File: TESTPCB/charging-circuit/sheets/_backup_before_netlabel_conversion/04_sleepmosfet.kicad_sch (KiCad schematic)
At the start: 8 parts, among them P3 1.27mm/1*3p, Q8 CJQ4435, U4 TPL5110DDCT

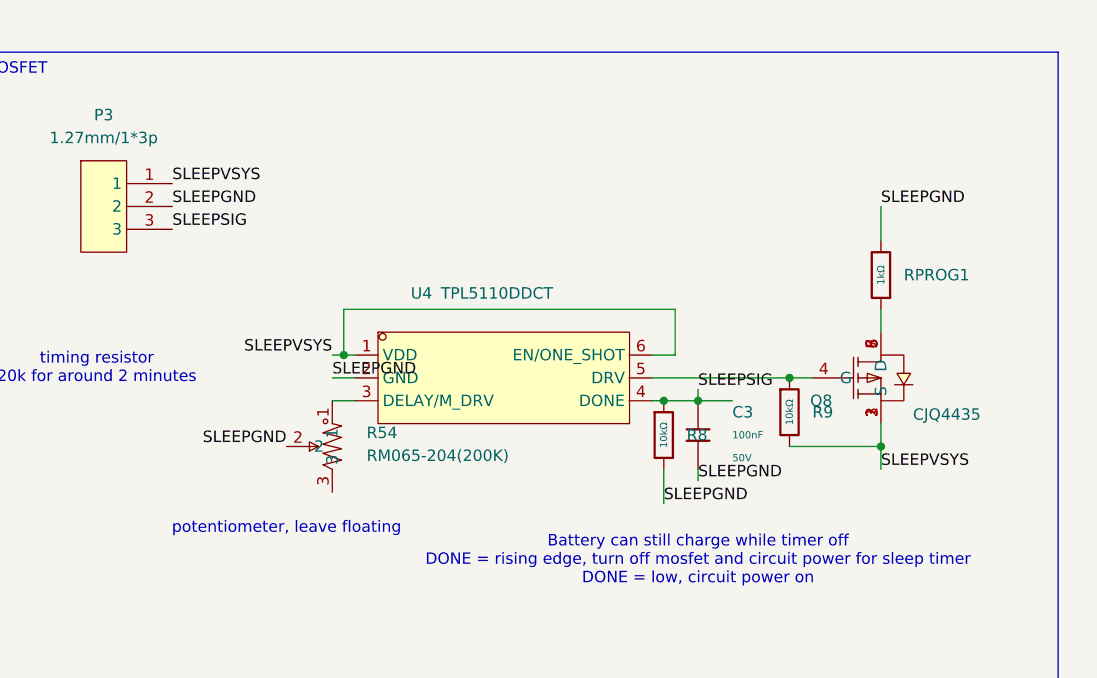
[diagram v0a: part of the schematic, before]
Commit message: Fixed formatting issues, now the hierachal sheets are all labeled as net labels and when we want to expose their pins we will make them into hierchal or global pins
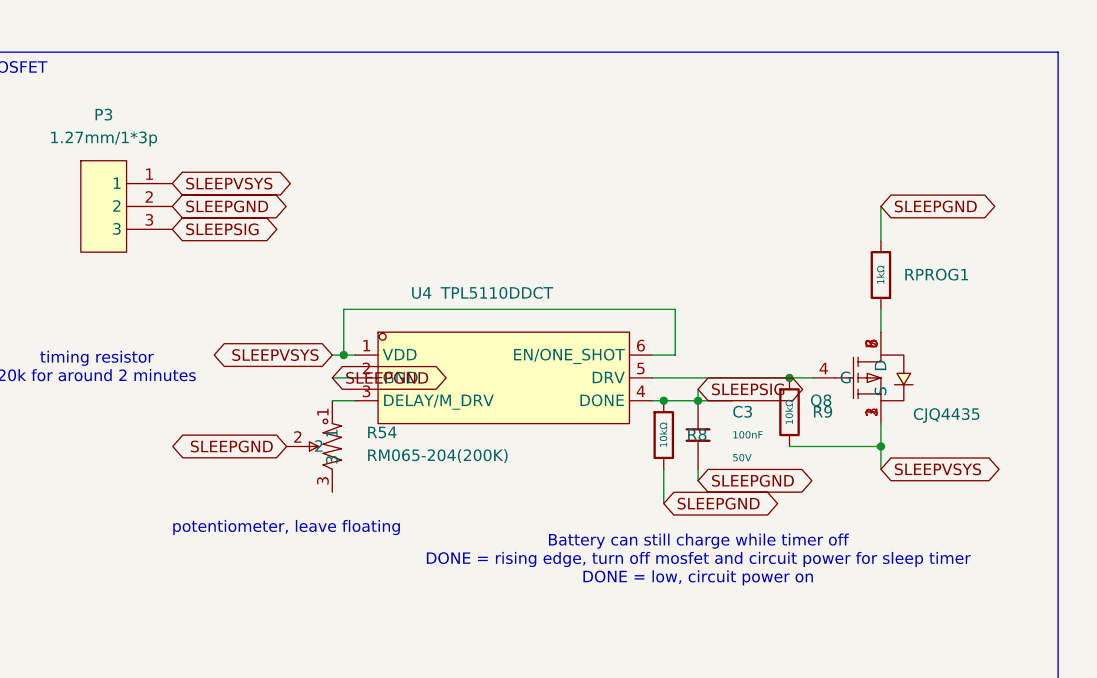
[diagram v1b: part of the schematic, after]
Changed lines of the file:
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@@
 		)
 	)
-	(label "SLEEPGND"
+	(global_label "SLEEPGND"
+		(shape bidirectional)
 		(at 186.69 90.17 0)
 		(effects
@@
 			(justify left bottom)
 		)
-	)
-	(label "SLEEPSIG"
+		(property "Intersheetrefs" "${INTERSHEET_REFS}"
+			(at 186.69 90.17 0)
+			(effects
+				(font
+					(size 1.27 1.27)
+				)
+				(hide yes)
+			)
+		)
+	)
+	(global_label "SLEEPSIG"
+		(shape bidirectional)
 		(at 166.37 110.49 0)
 		(effects
@@
 			(justify left bottom)
 		)
-	)
-	(label "SLEEPVSYS"
+		(property "Intersheetrefs" "${INTERSHEET_REFS}"
+			(at 166.37 110.49 0)
+			(effects
+				(font
+					(size 1.27 1.27)
+				)
+				(hide yes)
+			)
+		)
+	)
+	(global_label "SLEEPVSYS"
+		(shape bidirectional)
 		(at 107.95 87.63 0)
 		(effects
@@
 			(justify left bottom)
 		)
-	)
-	(label "SLEEPGND"
+		(property "Intersheetrefs" "${INTERSHEET_REFS}"
+			(at 107.95 87.63 0)
+			(effects
+				(font
+					(size 1.27 1.27)
+				)
+				(hide yes)
+			)
+		)
+	)
+	(global_label "SLEEPGND"
+		(shape bidirectional)
 		(at 107.95 90.17 0)
 		(effects
@@
 			(justify left bottom)
 		)
-	)
-	(label "SLEEPGND"
+		(property "Intersheetrefs" "${INTERSHEET_REFS}"
+			(at 107.95 90.17 0)
+			(effects
+				(font
+					(size 1.27 1.27)
+				)
+				(hide yes)
+			)
+		)
+	)
+	(global_label "SLEEPGND"
+		(shape bidirectional)
 		(at 120.65 116.84 180)
 		(effects
@@
 			(justify right bottom)
 		)
-	)
-	(label "SLEEPSIG"
+		(property "Intersheetrefs" "${INTERSHEET_REFS}"
+			(at 120.65 116.84 0)
+			(effects
+				(font
+					(size 1.27 1.27)
+				)
+				(hide yes)
+			)
+		)
+	)
+	(global_label "SLEEPSIG"
+		(shape bidirectional)
 		(at 107.95 92.71 0)
 		(effects
@@
 			(justify left bottom)
 		)
-	)
-	(label "SLEEPGND"
+		(property "Intersheetrefs" "${INTERSHEET_REFS}"
+			(at 107.95 92.71 0)
+			(effects
+				(font
+					(size 1.27 1.27)
+				)
+				(hide yes)
+			)
+		)
+	)
+	(global_label "SLEEPGND"
+		(shape bidirectional)
 		(at 125.73 109.22 0)
 		(effects
@@
 			(justify left bottom)
 		)
-	)
-	(label "SLEEPVSYS"
+		(property "Intersheetrefs" "${INTERSHEET_REFS}"
+			(at 125.73 109.22 0)
+			(effects
+				(font
+					(size 1.27 1.27)
+				)
+				(hide yes)
+			)
+		)
+	)
+	(global_label "SLEEPVSYS"
+		(shape bidirectional)
 		(at 125.73 106.68 180)
 		(effects
@@
 			(justify right bottom)
 		)
-	)
-	(label "SLEEPGND"
+		(property "Intersheetrefs" "${INTERSHEET_REFS}"
+			(at 125.73 106.68 0)
+			(effects
+				(font
+					(size 1.27 1.27)
+				)
+				(hide yes)
+			)
+		)
+	)
+	(global_label "SLEEPGND"
+		(shape bidirectional)
 		(at 162.56 123.19 0)
 		(effects
@@
 			(justify left bottom)
 		)
-	)
-	(label "SLEEPGND"
+		(property "Intersheetrefs" "${INTERSHEET_REFS}"
+			(at 162.56 123.19 0)
+			(effects
+				(font
+					(size 1.27 1.27)
+				)
+				(hide yes)
+			)
+		)
+	)
+	(global_label "SLEEPGND"
+		(shape bidirectional)
 		(at 166.37 120.65 0)
 		(effects
@@
 			(justify left bottom)
 		)
-	)
-	(label "SLEEPVSYS"
+		(property "Intersheetrefs" "${INTERSHEET_REFS}"
+			(at 166.37 120.65 0)
+			(effects
+				(font
+					(size 1.27 1.27)
+				)
+				(hide yes)
+			)
+		)
+	)
+	(global_label "SLEEPVSYS"
+		(shape bidirectional)
 		(at 186.69 119.38 0)
 		(effects
@@
 			(justify left bottom)
 		)
-	)
+		(property "Intersheetrefs" "${INTERSHEET_REFS}"
+			(at 186.69 119.38 0)
+			(effects
+				(font
+					(size 1.27 1.27)
+				)
+				(hide yes)
+			)
+		)
+	)
